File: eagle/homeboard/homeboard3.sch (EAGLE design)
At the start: 81 parts, among them IC1 XCF02S, IC2 25LC080SN, Q5 BC848SMD, Q6 BC848SMD, Q7 BC848SMD, Q8 BC848SMD, T1 BSS138, T2 BC848, T3 BSS138, U1 XC3S400TQ144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

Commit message: mah
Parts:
- renumbered JP1 to WR_PROT
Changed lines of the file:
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@@
 <part name="IC2" library="microchip" deviceset="25*" device="SN" technology="LC080"/>
 <part name="R47" library="rcl" deviceset="R-EU_" device="R0805" value="4K7"/>
-<part name="JP1" library="jumper" deviceset="JP1Q" device=""/>
+<part name="WR_PROT" library="jumper" deviceset="JP1Q" device=""/>
 <part name="R48" library="resistor" deviceset="R-EU_" device="M0805"/>
 <part name="C1" library="resistor" deviceset="C-EU" device="C0603"/>
@@
 <instance part="IC2" gate="G$1" x="-76.2" y="-121.92"/>
 <instance part="R47" gate="G$1" x="-104.14" y="-109.22" rot="R90"/>
-<instance part="JP1" gate="A" x="-104.14" y="-124.46"/>
+<instance part="WR_PROT" gate="A" x="-104.14" y="-124.46"/>
 <instance part="R48" gate="G$1" x="144.78" y="147.32"/>
 <instance part="C1" gate="G$1" x="132.08" y="142.24" rot="R180"/>
@@
 <junction x="-66.04" y="-132.08"/>
 <wire x1="-66.04" y1="-137.16" x2="-104.14" y2="-137.16" width="0.1524" layer="91"/>
-<pinref part="JP1" gate="A" pin="1"/>
+<pinref part="WR_PROT" gate="A" pin="1"/>
 <wire x1="-104.14" y1="-137.16" x2="-104.14" y2="-132.08" width="0.1524" layer="91"/>
 </segment>
@@
 <wire x1="-104.14" y1="-114.3" x2="-88.9" y2="-114.3" width="0.1524" layer="91"/>
 <pinref part="R47" gate="G$1" pin="1"/>
-<pinref part="JP1" gate="A" pin="2"/>
+<pinref part="WR_PROT" gate="A" pin="2"/>
 <wire x1="-104.14" y1="-116.84" x2="-104.14" y2="-114.3" width="0.1524" layer="91"/>
 <junction x="-104.14" y="-114.3"/>

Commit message: mah
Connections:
- net MISO: now also U1B4.IO_L27P_4D1
- net MOSI: now also U1B4.IO_L01N_4VRP_4
- net SCLK: now also U1B4.IOVREF_4
- net SPI_SEL0: now also U1B4.IO_L01P_4VRN_4
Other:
- moved on the sheet: IC2, R47, WR_PROT
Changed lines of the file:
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@@
 <instance part="SUPPLY4" gate="GND" x="83.82" y="-27.94"/>
 <instance part="SUPPLY5" gate="GND" x="83.82" y="17.78"/>
-<instance part="IC2" gate="G$1" x="-76.2" y="-121.92"/>
-<instance part="R47" gate="G$1" x="-104.14" y="-109.22" rot="R90"/>
-<instance part="WR_PROT" gate="A" x="-104.14" y="-124.46"/>
+<instance part="IC2" gate="G$1" x="248.92" y="-78.74"/>
+<instance part="R47" gate="G$1" x="220.98" y="-66.04" rot="R90"/>
+<instance part="WR_PROT" gate="A" x="220.98" y="-81.28"/>
 <instance part="R48" gate="G$1" x="144.78" y="147.32"/>
 <instance part="C1" gate="G$1" x="132.08" y="142.24" rot="R180"/>
@@
 <segment>
 <pinref part="IC2" gate="G$1" pin="GND"/>
-<wire x1="-55.88" y1="-132.08" x2="-66.04" y2="-132.08" width="0.1524" layer="91"/>
-<label x="-60.96" y="-132.08" size="1.778" layer="95"/>
-<wire x1="-66.04" y1="-132.08" x2="-68.58" y2="-132.08" width="0.1524" layer="91"/>
-<wire x1="-66.04" y1="-132.08" x2="-66.04" y2="-137.16" width="0.1524" layer="91"/>
-<junction x="-66.04" y="-132.08"/>
-<wire x1="-66.04" y1="-137.16" x2="-104.14" y2="-137.16" width="0.1524" layer="91"/>
+<wire x1="269.24" y1="-88.9" x2="259.08" y2="-88.9" width="0.1524" layer="91"/>
+<label x="264.16" y="-88.9" size="1.778" layer="95"/>
+<wire x1="259.08" y1="-88.9" x2="256.54" y2="-88.9" width="0.1524" layer="91"/>
+<wire x1="259.08" y1="-88.9" x2="259.08" y2="-93.98" width="0.1524" layer="91"/>
+<junction x="259.08" y="-88.9"/>
+<wire x1="259.08" y1="-93.98" x2="220.98" y2="-93.98" width="0.1524" layer="91"/>
 <pinref part="WR_PROT" gate="A" pin="1"/>
-<wire x1="-104.14" y1="-137.16" x2="-104.14" y2="-132.08" width="0.1524" layer="91"/>
+<wire x1="220.98" y1="-93.98" x2="220.98" y2="-88.9" width="0.1524" layer="91"/>
 </segment>
 <segment>
@@
 <segment>
 <pinref part="IC2" gate="G$1" pin="VCC"/>
-<wire x1="-68.58" y1="-109.22" x2="-66.04" y2="-109.22" width="0.1524" layer="91"/>
-<label x="-60.96" y="-109.22" size="1.778" layer="95"/>
+<wire x1="256.54" y1="-66.04" x2="259.08" y2="-66.04" width="0.1524" layer="91"/>
+<label x="264.16" y="-66.04" size="1.778" layer="95"/>
 <pinref part="R47" gate="G$1" pin="2"/>
-<wire x1="-66.04" y1="-109.22" x2="-55.88" y2="-109.22" width="0.1524" layer="91"/>
-<wire x1="-104.14" y1="-104.14" x2="-66.04" y2="-104.14" width="0.1524" layer="91"/>
-<wire x1="-66.04" y1="-104.14" x2="-66.04" y2="-109.22" width="0.1524" layer="91"/>
-<junction x="-66.04" y="-109.22"/>
+<wire x1="259.08" y1="-66.04" x2="269.24" y2="-66.04" width="0.1524" layer="91"/>
+<wire x1="220.98" y1="-60.96" x2="259.08" y2="-60.96" width="0.1524" layer="91"/>
+<wire x1="259.08" y1="-60.96" x2="259.08" y2="-66.04" width="0.1524" layer="91"/>
+<junction x="259.08" y="-66.04"/>
 </segment>
 <segment>
 <pinref part="IC2" gate="G$1" pin="!HOLD"/>
-<label x="-96.52" y="-127" size="1.778" layer="95"/>
-<wire x1="-96.52" y1="-127" x2="-88.9" y2="-127" width="0.1524" layer="91"/>
+<label x="228.6" y="-83.82" size="1.778" layer="95"/>
+<wire x1="228.6" y1="-83.82" x2="236.22" y2="-83.82" width="0.1524" layer="91"/>
 </segment>
 <segment>
@@
 <segment>
 <pinref part="U1" gate="B4" pin="IO_L31N_4INIT_B"/>
-<wire x1="175.26" y1="-40.64" x2="175.26" y2="-50.8" width="0.1524" layer="91"/>
-<wire x1="175.26" y1="-50.8" x2="185.42" y2="-50.8" width="0.1524" layer="91"/>
-<label x="180.34" y="-50.8" size="1.778" layer="95"/>
+<wire x1="175.26" y1="-40.64" x2="175.26" y2="-63.5" width="0.1524" layer="91"/>
+<wire x1="175.26" y1="-63.5" x2="185.42" y2="-63.5" width="0.1524" layer="91"/>
+<label x="180.34" y="-63.5" size="1.778" layer="95"/>
 </segment>
 </net>
@@
 <segment>
 <pinref part="U1" gate="B4" pin="IO_L27N_4DIND0"/>
-<wire x1="172.72" y1="-40.64" x2="172.72" y2="-53.34" width="0.1524" layer="91"/>
-<wire x1="172.72" y1="-53.34" x2="185.42" y2="-53.34" width="0.1524" layer="91"/>
-<label x="180.34" y="-53.34" size="1.778" layer="95"/>
+<wire x1="172.72" y1="-40.64" x2="172.72" y2="-60.96" width="0.1524" layer="91"/>
+<wire x1="172.72" y1="-60.96" x2="185.42" y2="-60.96" width="0.1524" layer="91"/>
+<label x="180.34" y="-60.96" size="1.778" layer="95"/>
 </segment>
 </net>
@@
 <segment>
 <pinref part="IC2" gate="G$1" pin="SCK"/>
-<wire x1="-96.52" y1="-124.46" x2="-88.9" y2="-124.46" width="0.1524" layer="91"/>
-<label x="-96.52" y="-124.46" size="1.778" layer="95"/>
+<wire x1="228.6" y1="-81.28" x2="236.22" y2="-81.28" width="0.1524" layer="91"/>
+<label x="228.6" y="-81.28" size="1.778" layer="95"/>
 </segment>
 <segment>
@@
 <label x="-127" y="-144.78" size="1.778" layer="95"/>
 </segment>
+<segment>
+<pinref part="U1" gate="B4" pin="IOVREF_4"/>
+<wire x1="185.42" y1="-53.34" x2="157.48" y2="-53.34" width="0.1524" layer="91"/>
+<wire x1="157.48" y1="-53.34" x2="157.48" y2="-40.64" width="0.1524" layer="91"/>
+<label x="185.42" y="-53.34" size="1.778" layer="95"/>
+</segment>
 </net>
 <net name="MOSI" class="0">
 <segment>
 <pinref part="IC2" gate="G$1" pin="SI"/>
-<wire x1="-96.52" y1="-121.92" x2="-88.9" y2="-121.92" width="0.1524" layer="91"/>
-<label x="-96.52" y="-121.92" size="1.778" layer="95"/>
+<wire x1="228.6" y1="-78.74" x2="236.22" y2="-78.74" width="0.1524" layer="91"/>
+<label x="228.6" y="-78.74" size="1.778" layer="95"/>
 </segment>
 <segment>
@@
 <label x="-127" y="-142.24" size="1.778" layer="95"/>
 </segment>
+<segment>
+<pinref part="U1" gate="B4" pin="IO_L01N_4VRP_4"/>
+<wire x1="185.42" y1="-55.88" x2="180.34" y2="-55.88" width="0.1524" layer="91"/>
+<wire x1="180.34" y1="-55.88" x2="180.34" y2="-40.64" width="0.1524" layer="91"/>
+<label x="185.42" y="-55.88" size="1.778" layer="95"/>
+</segment>
 </net>
 <net name="MISO" class="0">
 <segment>
 <pinref part="IC2" gate="G$1" pin="SO"/>
-<wire x1="-55.88" y1="-121.92" x2="-60.96" y2="-121.92" width="0.1524" layer="91"/>
-<label x="-60.96" y="-121.92" size="1.778" layer="95"/>
+<wire x1="269.24" y1="-78.74" x2="264.16" y2="-78.74" width="0.1524" layer="91"/>
+<label x="264.16" y="-78.74" size="1.778" layer="95"/>
 </segment>
 <segment>
@@
 <label x="-127" y="-139.7" size="1.778" layer="95"/>
 </segment>
+<segment>
+<pinref part="U1" gate="B4" pin="IO_L27P_4D1"/>
+<wire x1="185.42" y1="-66.04" x2="170.18" y2="-66.04" width="0.1524" layer="91"/>
+<wire x1="170.18" y1="-66.04" x2="170.18" y2="-40.64" width="0.1524" layer="91"/>
+<label x="185.42" y="-66.04" size="1.778" layer="95"/>
+</segment>
 </net>
 <net name="SPI_SEL0" class="0">
 <segment>
 <pinref part="IC2" gate="G$1" pin="!CS"/>
-<wire x1="-96.52" y1="-119.38" x2="-88.9" y2="-119.38" width="0.1524" layer="91"/>
-<label x="-96.52" y="-119.38" size="1.778" layer="95"/>
+<wire x1="228.6" y1="-76.2" x2="236.22" y2="-76.2" width="0.1524" layer="91"/>
+<label x="228.6" y="-76.2" size="1.778" layer="95"/>
+</segment>
+<segment>
+<pinref part="U1" gate="B4" pin="IO_L01P_4VRN_4"/>
+<wire x1="185.42" y1="-58.42" x2="182.88" y2="-58.42" width="0.1524" layer="91"/>
+<wire x1="182.88" y1="-58.42" x2="182.88" y2="-40.64" width="0.1524" layer="91"/>
+<label x="185.42" y="-58.42" size="1.778" layer="95"/>
 </segment>
 </net>
@@
 <segment>
 <pinref part="IC2" gate="G$1" pin="!WP"/>
-<wire x1="-104.14" y1="-114.3" x2="-88.9" y2="-114.3" width="0.1524" layer="91"/>
+<wire x1="220.98" y1="-71.12" x2="236.22" y2="-71.12" width="0.1524" layer="91"/>
 <pinref part="R47" gate="G$1" pin="1"/>
 <pinref part="WR_PROT" gate="A" pin="2"/>
-<wire x1="-104.14" y1="-116.84" x2="-104.14" y2="-114.3" width="0.1524" layer="91"/>
-<junction x="-104.14" y="-114.3"/>
-</segment>
-</net>
+<wire x1="220.98" y1="-73.66" x2="220.98" y2="-71.12" width="0.1524" layer="91"/>
+<junction x="220.98" y="-71.12"/>
+</segment>
+</net>

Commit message: stuff
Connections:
- new net N$71: U1B4.IO_L31P_4DOUTBUSY
- new net N$75: U1B5.IO_L32P_5GCLK2
- new net N$76: U1B4.IO_L32P_4GCLK0
- net FPGA_AUDIO_LEFT: now also U1B4.IO_L30P_4D3
- net FPGA_AUDIO_RIGHT: now also U1B4.IO_L30N_4D2
- net N$50: now also U1B4.IO_L32N_4GCLK1; no longer U$2.OUT, U1B5.IO_L32P_5GCLK2
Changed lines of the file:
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@@
-</segment>
-</net>
-<net name="N$50" class="0">
-<segment>
-<pinref part="U$2" gate="G$1" pin="OUT"/>
-<wire x1="162.56" y1="-68.58" x2="162.56" y2="-154.94" width="0.1524" layer="91"/>
-<pinref part="U1" gate="B5" pin="IO_L32P_5GCLK2"/>
-<wire x1="132.08" y1="-40.64" x2="132.08" y2="-68.58" width="0.1524" layer="91"/>
-<wire x1="132.08" y1="-68.58" x2="162.56" y2="-68.58" width="0.1524" layer="91"/>
 </segment>
 </net>
@@
 <label x="106.68" y="-63.5" size="1.778" layer="95"/>
 </segment>
+<segment>
+<pinref part="U1" gate="B4" pin="IO_L30P_4D3"/>
+<wire x1="185.42" y1="-71.12" x2="165.1" y2="-71.12" width="0.1524" layer="91"/>
+<wire x1="165.1" y1="-71.12" x2="165.1" y2="-40.64" width="0.1524" layer="91"/>
+<label x="185.42" y="-71.12" size="1.778" layer="95"/>
+</segment>
 </net>
 <net name="FPGA_AUDIO_RIGHT" class="0">
@@
 <wire x1="134.62" y1="-66.04" x2="134.62" y2="-40.64" width="0.1524" layer="91"/>
 <label x="106.68" y="-66.04" size="1.778" layer="95"/>
+</segment>
+<segment>
+<pinref part="U1" gate="B4" pin="IO_L30N_4D2"/>
+<wire x1="185.42" y1="-68.58" x2="167.64" y2="-68.58" width="0.1524" layer="91"/>
+<wire x1="167.64" y1="-68.58" x2="167.64" y2="-40.64" width="0.1524" layer="91"/>
+<label x="185.42" y="-68.58" size="1.778" layer="95"/>
 </segment>
 </net>
@@
 </segment>
 </net>
+<net name="N$75" class="0">
+<segment>
+<pinref part="U1" gate="B5" pin="IO_L32P_5GCLK2"/>
+<wire x1="132.08" y1="-40.64" x2="132.08" y2="-68.58" width="0.1524" layer="91"/>
+</segment>
+</net>
+<net name="N$50" class="0">
+<segment>
+<pinref part="U1" gate="B4" pin="IO_L32N_4GCLK1"/>
+<wire x1="185.42" y1="-76.2" x2="160.02" y2="-76.2" width="0.1524" layer="91"/>
+<wire x1="160.02" y1="-76.2" x2="160.02" y2="-40.64" width="0.1524" layer="91"/>
+<label x="185.42" y="-76.2" size="1.778" layer="95"/>
+</segment>
+</net>
+<net name="N$76" class="0">
+<segment>
+<wire x1="185.42" y1="-78.74" x2="162.56" y2="-78.74" width="0.1524" layer="91"/>
+<wire x1="162.56" y1="-78.74" x2="162.56" y2="-40.64" width="0.1524" layer="91"/>
+<pinref part="U1" gate="B4" pin="IO_L32P_4GCLK0"/>
+<label x="185.42" y="-78.74" size="1.778" layer="95"/>
+</segment>
+</net>
+<net name="N$71" class="0">
+<segment>
+<pinref part="U1" gate="B4" pin="IO_L31P_4DOUTBUSY"/>
+<wire x1="185.42" y1="-73.66" x2="177.8" y2="-73.66" width="0.1524" layer="91"/>
+<wire x1="177.8" y1="-73.66" x2="177.8" y2="-40.64" width="0.1524" layer="91"/>
+<label x="185.42" y="-73.66" size="1.778" layer="95"/>
+</segment>
+</net>

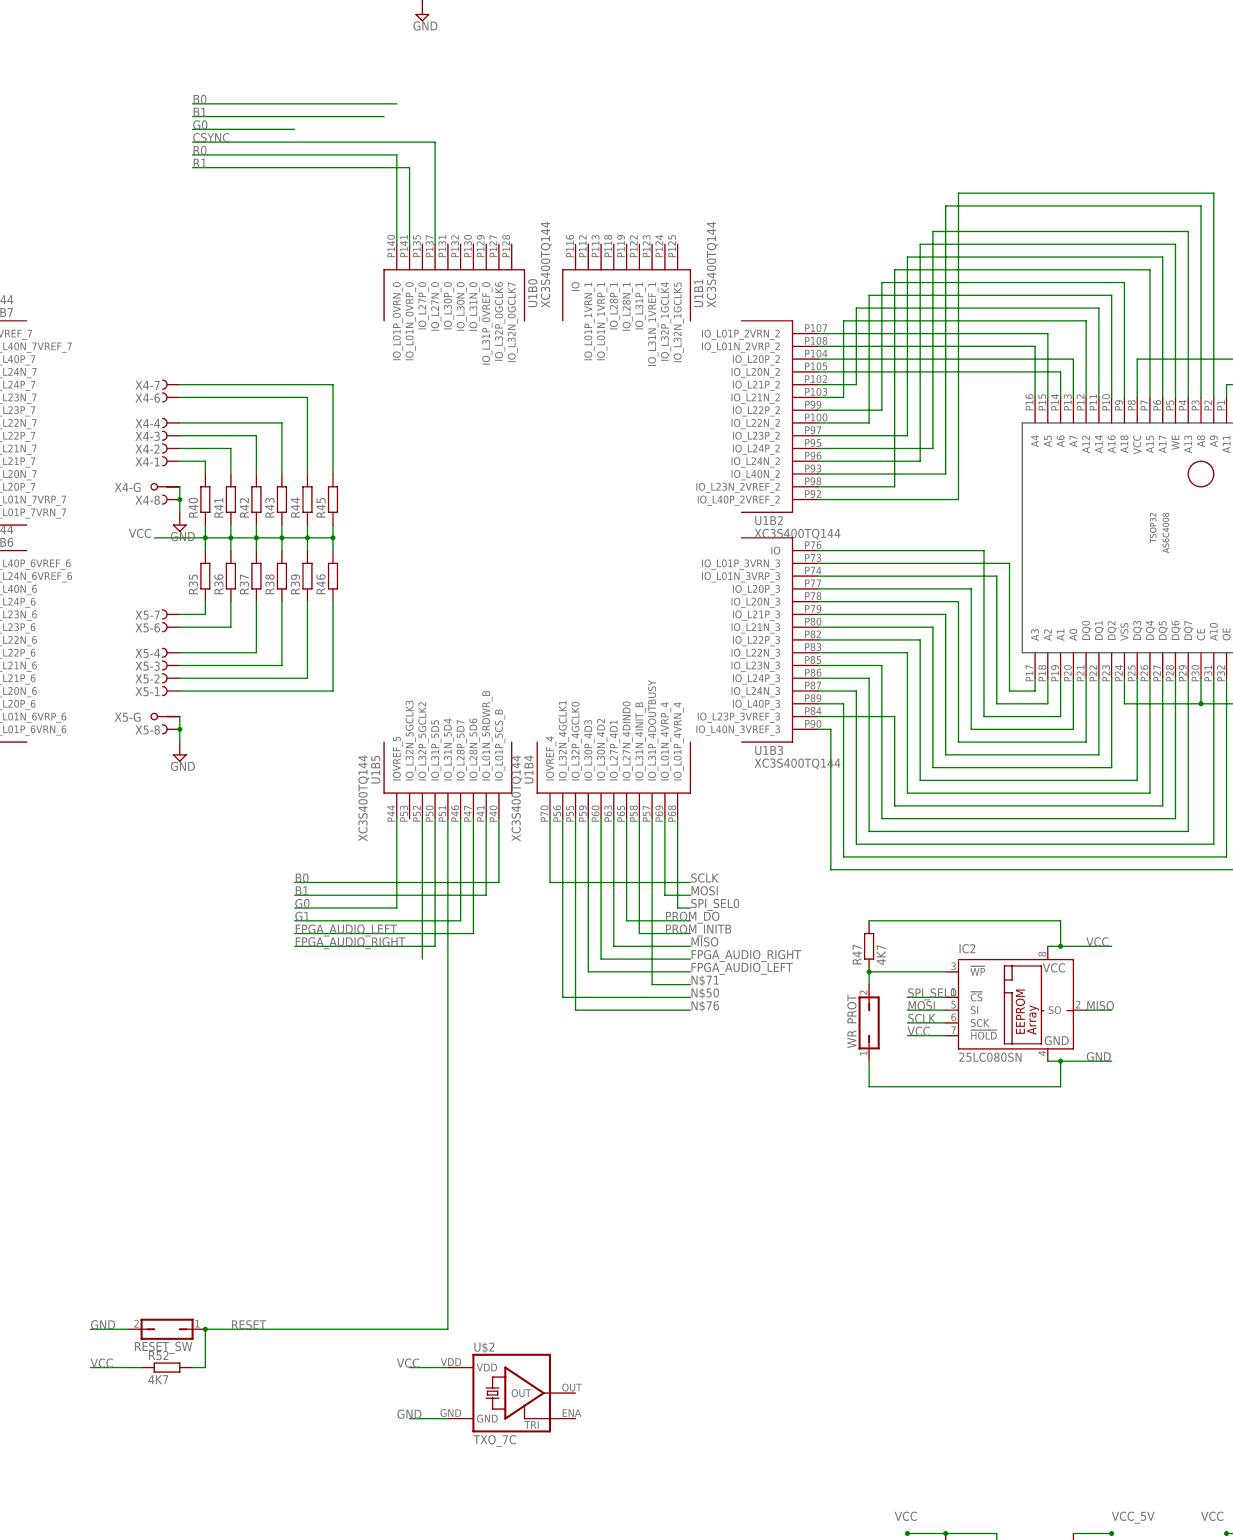
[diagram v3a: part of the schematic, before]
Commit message: scart and xtal all wired up, not butted up tho
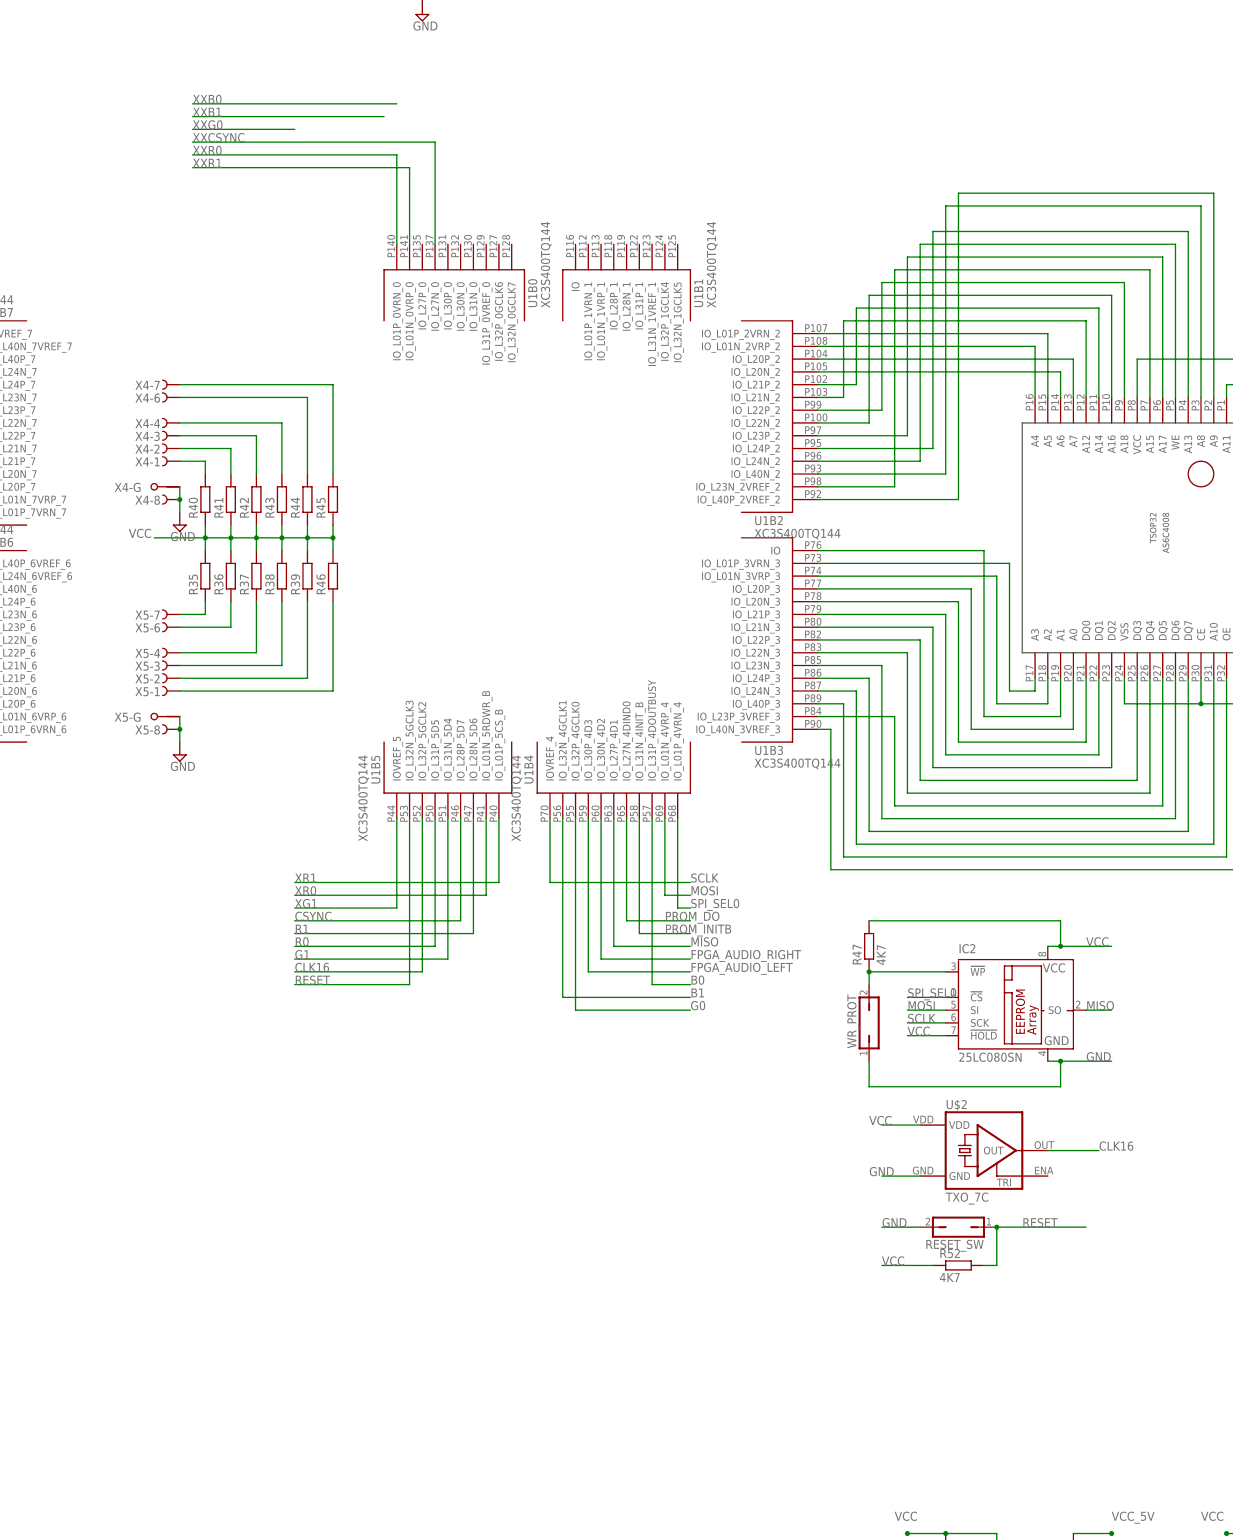
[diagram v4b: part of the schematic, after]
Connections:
- removed net N$50: U1B4.IO_L32N_4GCLK1
- removed net N$71: U1B4.IO_L31P_4DOUTBUSY
- removed net N$75: U1B5.IO_L32P_5GCLK2
- removed net N$76: U1B4.IO_L32P_4GCLK0
- new net CLK16: U$2.OUT, U1B5.IO_L32P_5GCLK2
- new net XG1: U1B5.IOVREF_5
- new net XR0: U1B5.IO_L01N_5RDWR_B
- new net XR1: U1B5.IO_L01P_5CS_B
- new net XXCSYNC: U1B0.IO_L27N_0
- new net XXR0: U1B0.IO_L01P_0VRN_0
- new net XXR1: U1B0.IO_L01N_0VRP_0
- net B0: now also U1B4.IO_L31P_4DOUTBUSY; no longer U1B5.IO_L01P_5CS_B
- net B1: now also U1B4.IO_L32N_4GCLK1; no longer U1B5.IO_L01N_5RDWR_B
- net CSYNC: now also U1B5.IO_L28P_5D7; no longer U1B0.IO_L27N_0
- net FPGA_AUDIO_LEFT: no longer U1B5.IO_L28N_5D6
- net FPGA_AUDIO_RIGHT: no longer U1B5.IO_L31P_5D5
- net G0: now also U1B4.IO_L32P_4GCLK0; no longer U1B5.IOVREF_5
- net G1: now also U1B5.IO_L31N_5D4; no longer U1B5.IO_L28P_5D7
- net R0: now also U1B5.IO_L31P_5D5; no longer U1B0.IO_L01P_0VRN_0
- net R1: now also U1B5.IO_L28N_5D6; no longer U1B0.IO_L01N_0VRP_0
- net RESET: now also U1B5.IO_L32N_5GCLK3; no longer U1B5.IO_L31N_5D4
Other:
- moved on the sheet: R52, RESET_SW, U$2
